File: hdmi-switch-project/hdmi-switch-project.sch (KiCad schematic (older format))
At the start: 0 parts

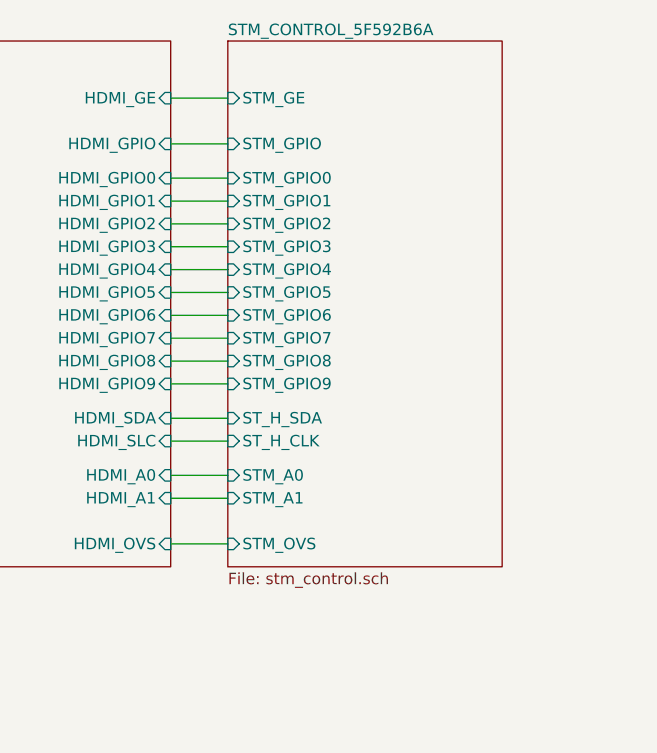
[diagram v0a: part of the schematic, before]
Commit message: added OVS jumper
Signed-off-by: Andrej Manduch <amanduch@gmail.com>
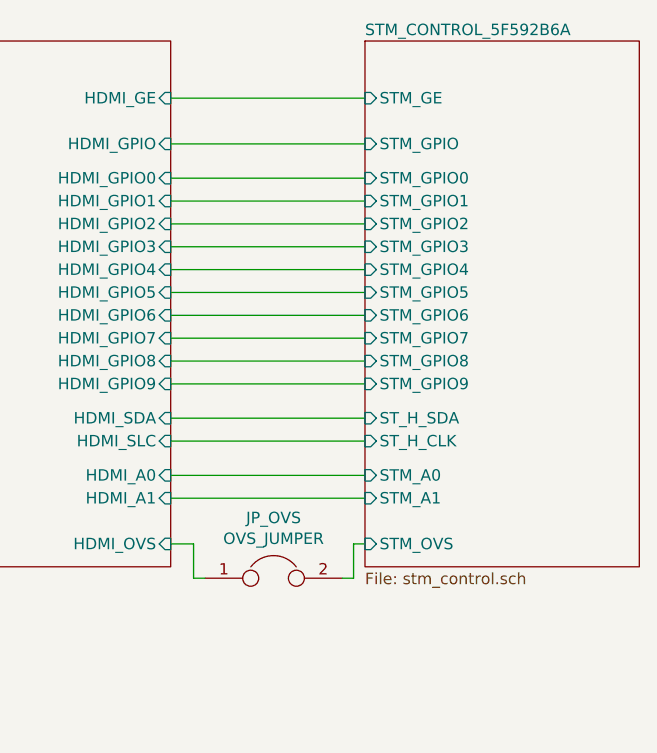
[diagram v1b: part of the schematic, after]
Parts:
- added JP_OVS: OVS_JUMPER, symbol Device:Jumper
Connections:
- net HDMI_CIRCUIT_F9FB5DE/HDMI_OVS: now also JP_OVS.1
- new net STM_CONTROL_5F592B6A/STM_OVS: JP_OVS.2
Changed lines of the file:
@@
 $EndSheet
 Wire Wire Line
-	6300 3050 6050 3050
+	6900 3050 6050 3050
 Wire Wire Line
-	6050 3150 6300 3150
+	6050 3150 6900 3150
 Wire Wire Line
-	6300 2900 6050 2900
+	6900 2900 6050 2900
 Wire Wire Line
-	6050 2800 6300 2800
+	6050 2800 6900 2800
 Wire Wire Line
-	6300 2450 6050 2450
+	6900 2450 6050 2450
 Wire Wire Line
-	6050 2350 6300 2350
+	6050 2350 6900 2350
 Wire Wire Line
-	6300 2250 6050 2250
+	6900 2250 6050 2250
 Wire Wire Line
-	6050 2150 6300 2150
+	6050 2150 6900 2150
 Wire Wire Line
-	6300 2050 6050 2050
+	6900 2050 6050 2050
 Wire Wire Line
-	6050 1950 6300 1950
+	6050 1950 6900 1950
 Wire Wire Line
-	6300 1850 6050 1850
+	6900 1850 6050 1850
 Wire Wire Line
-	6050 1750 6300 1750
+	6050 1750 6900 1750
 Wire Wire Line
-	6300 1600 6050 1600
+	6900 1600 6050 1600
 Wire Wire Line
-	6050 1400 6300 1400
+	6050 1400 6900 1400
 $Sheet
-S 6300 1150 1200 2300
+S 6900 1150 1200 2300
 U 5F592B6A
 F0 "STM_CONTROL_5F592B6A" 50
 F1 "stm_control.sch" 50
-F2 "ST_H_CLK" I L 6300 2900 50
-F3 "ST_H_SDA" I L 6300 2800 50
-F4 "STM_GPIO0" I L 6300 1750 50
-F5 "STM_GPIO1" I L 6300 1850 50
-F6 "STM_GPIO2" I L 6300 1950 50
-F7 "STM_GPIO3" I L 6300 2050 50
-F8 "STM_GPIO4" I L 6300 2150 50
-F9 "STM_GPIO5" I L 6300 2250 50
-F10 "STM_GPIO6" I L 6300 2350 50
-F11 "STM_GPIO7" I L 6300 2450 50
-F12 "STM_GPIO" I L 6300 1600 50
-F13 "STM_GE" I L 6300 1400 50
-F14 "STM_A0" I L 6300 3050 50
-F15 "STM_A1" I L 6300 3150 50
-F16 "STM_GPIO8" I L 6300 2550 50
-F17 "STM_GPIO9" I L 6300 2650 50
-F18 "STM_OVS" I L 6300 3350 50
+F2 "ST_H_CLK" I L 6900 2900 50
+F3 "ST_H_SDA" I L 6900 2800 50
+F4 "STM_GPIO0" I L 6900 1750 50
+F5 "STM_GPIO1" I L 6900 1850 50
+F6 "STM_GPIO2" I L 6900 1950 50
+F7 "STM_GPIO3" I L 6900 2050 50
+F8 "STM_GPIO4" I L 6900 2150 50
+F9 "STM_GPIO5" I L 6900 2250 50
+F10 "STM_GPIO6" I L 6900 2350 50
+F11 "STM_GPIO7" I L 6900 2450 50
+F12 "STM_GPIO" I L 6900 1600 50
+F13 "STM_GE" I L 6900 1400 50
+F14 "STM_A0" I L 6900 3050 50
+F15 "STM_A1" I L 6900 3150 50
+F16 "STM_GPIO8" I L 6900 2550 50
+F17 "STM_GPIO9" I L 6900 2650 50
+F18 "STM_OVS" I L 6900 3350 50
 $EndSheet
 Wire Wire Line
-	6300 3350 6050 3350
+	6050 2650 6900 2650
 Wire Wire Line
-	6050 2650 6300 2650
-Wire Wire Line
-	6300 2550 6050 2550
+	6900 2550 6050 2550
 $Comp
 L power:GND #PWR?
@@
 Wire Wire Line
 	3000 4150 3000 4200
+$Comp
+L Device:Jumper JP_OVS
+U 1 1 60C790A5
+P 6500 3500
+F 0 "JP_OVS" H 6500 3764 50  0000 C CNN
+F 1 "OVS_JUMPER" H 6500 3673 50  0000 C CNN
+F 2 "" H 6500 3500 50  0001 C CNN
+F 3 "~" H 6500 3500 50  0001 C CNN
+	1    6500 3500
+	1    0    0    -1
+$EndComp
+Wire Wire Line
+	6800 3500 6850 3500
+Wire Wire Line
+	6850 3500 6850 3350
+Wire Wire Line
+	6850 3350 6900 3350
+Wire Wire Line
+	6200 3500 6150 3500
+Wire Wire Line
+	6150 3500 6150 3350
+Wire Wire Line
+	6150 3350 6050 3350
 $EndSCHEMATC

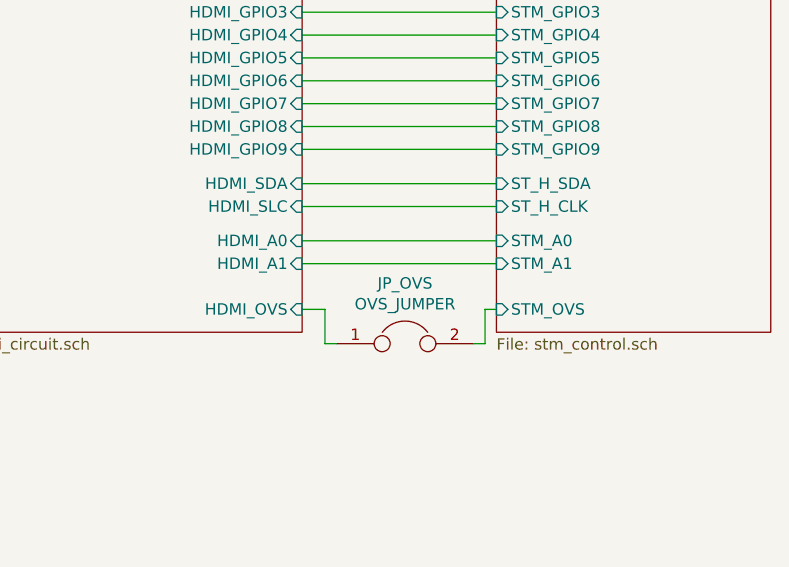
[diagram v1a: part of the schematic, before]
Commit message: Cosmetical changes, and VSDJ pin fixup
Signed-off-by: Andrej Manduch <amanduch@gmail.com>
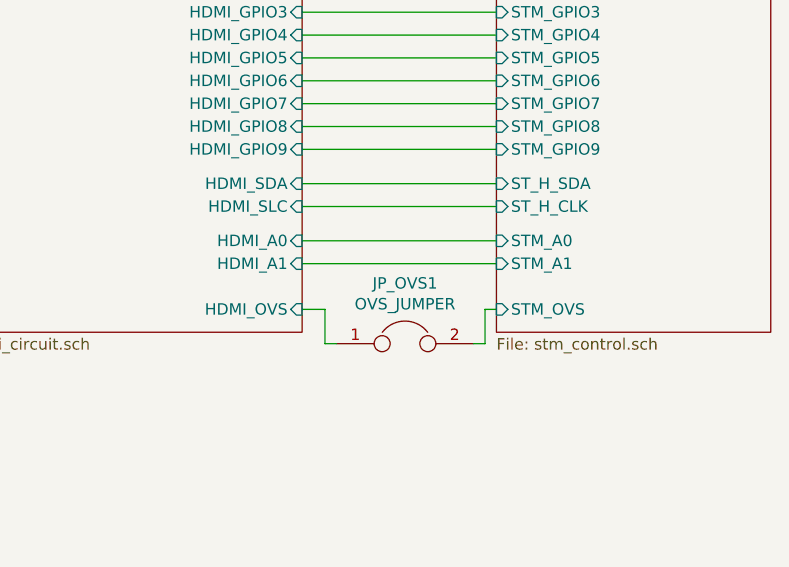
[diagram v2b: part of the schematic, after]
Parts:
- renumbered JP_OVS to JP_OVS1
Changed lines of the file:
@@
 EELAYER 30 0
 EELAYER END
-$Descr A3 11693 16535 portrait
+$Descr A3 16535 11693
 encoding utf-8
 Sheet 1 4
-Title ""
-Date ""
+Title "HDMI Switch 4:2 modul"
+Date "2020-06-30"
 Rev ""
 Comp ""
-Comment1 ""
+Comment1 "Devel board"
 Comment2 ""
 Comment3 ""
@@
 	6900 2550 6050 2550
 $Comp
-L power:GND #PWR?
+L power:GND #PWR0101
 U 1 1 60C19124
 P 3000 4200
-F 0 "#PWR?" H 3000 3950 50  0001 C CNN
+F 0 "#PWR0101" H 3000 3950 50  0001 C CNN
 F 1 "GND" H 3005 4027 50  0000 C CNN
 F 2 "" H 3000 4200 50  0001 C CNN
@@
 	3000 4150 3000 4200
 $Comp
-L Device:Jumper JP_OVS
+L Device:Jumper JP_OVS1
 U 1 1 60C790A5
 P 6500 3500
-F 0 "JP_OVS" H 6500 3764 50  0000 C CNN
+F 0 "JP_OVS1" H 6500 3764 50  0000 C CNN
 F 1 "OVS_JUMPER" H 6500 3673 50  0000 C CNN
 F 2 "" H 6500 3500 50  0001 C CNN

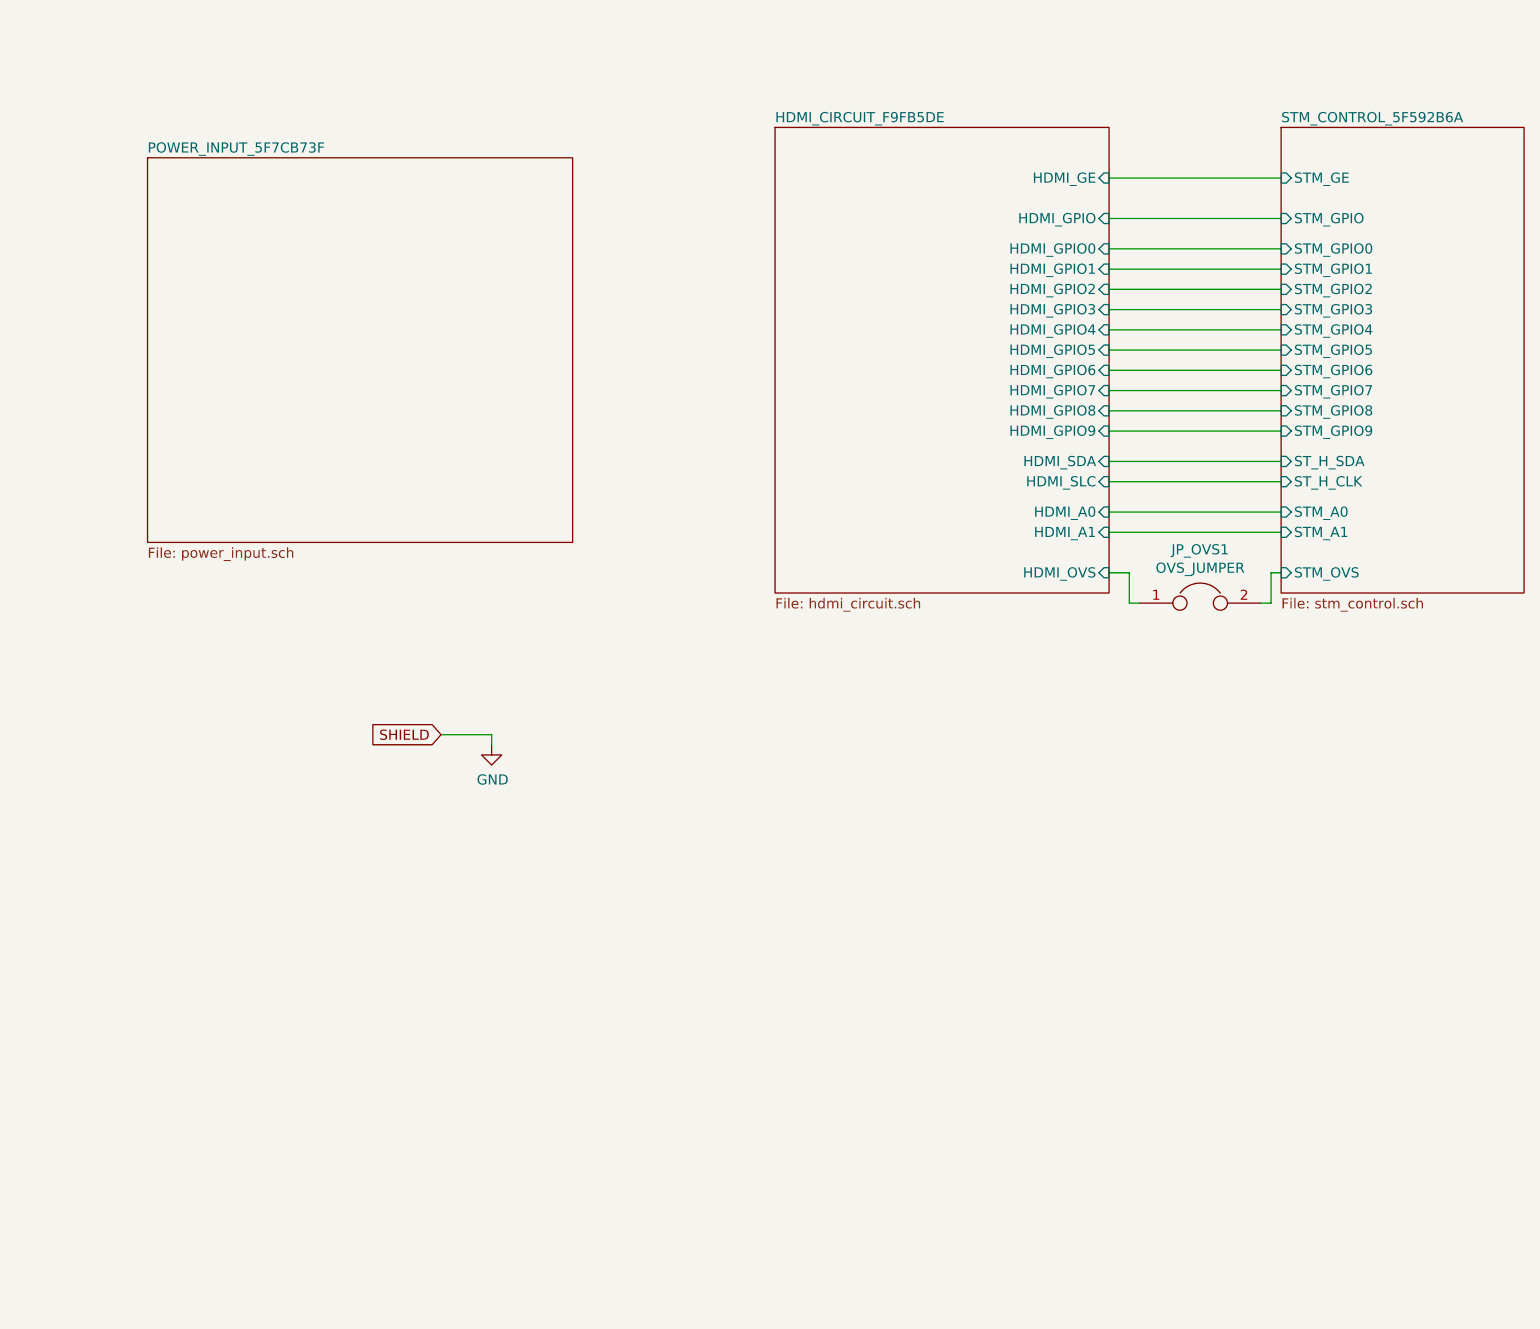
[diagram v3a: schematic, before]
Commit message: Added 2k resistor between GPIO ports
Signed-off-by: Andrej Manduch <amanduch@gmail.com>
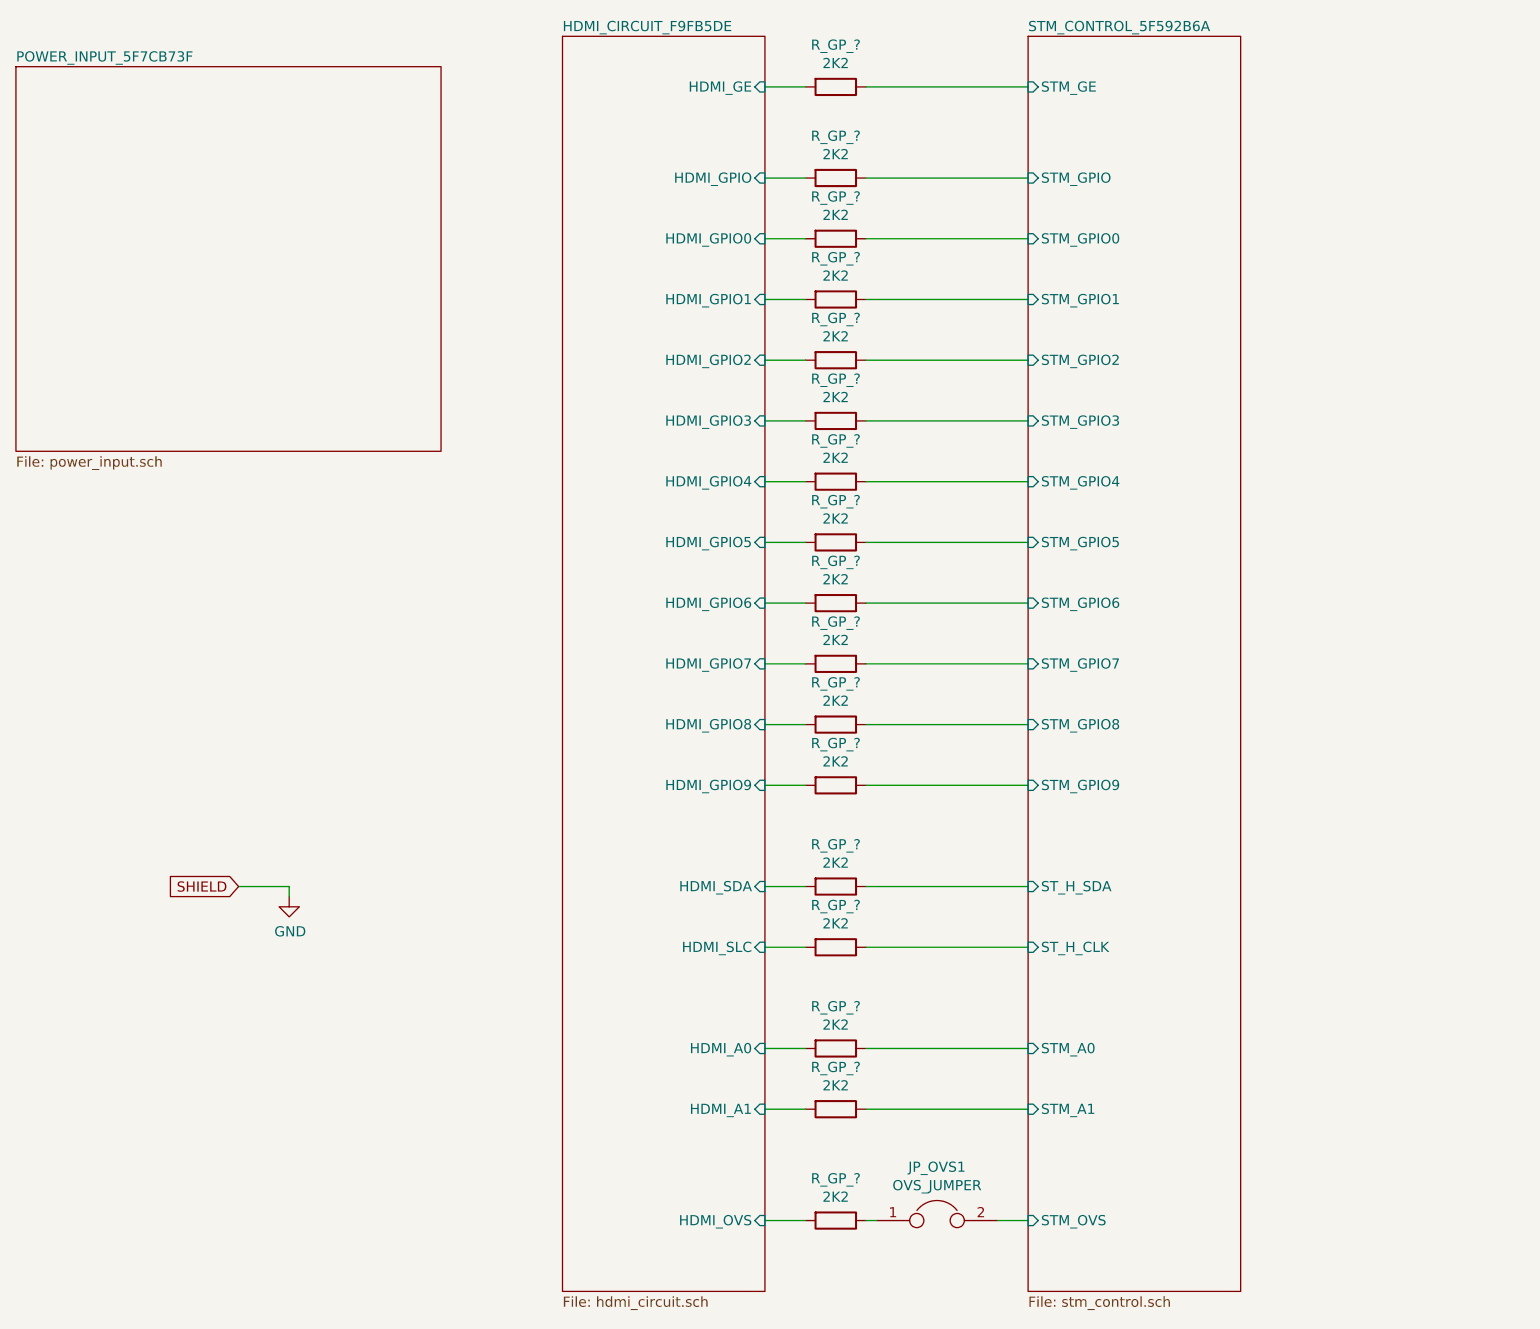
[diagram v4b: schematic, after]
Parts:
- added R_GP_? (x17): 2K2, symbol Device:R
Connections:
- net HDMI_CIRCUIT_F9FB5DE/HDMI_A0: now also R_GP_?.2
- net HDMI_CIRCUIT_F9FB5DE/HDMI_A1: now also R_GP_?.2
- net HDMI_CIRCUIT_F9FB5DE/HDMI_GE: now also R_GP_?.2
- net HDMI_CIRCUIT_F9FB5DE/HDMI_GPIO: now also R_GP_?.2
- net HDMI_CIRCUIT_F9FB5DE/HDMI_GPIO0: now also R_GP_?.2
- net HDMI_CIRCUIT_F9FB5DE/HDMI_GPIO1: now also R_GP_?.2
- net HDMI_CIRCUIT_F9FB5DE/HDMI_GPIO2: now also R_GP_?.2
- net HDMI_CIRCUIT_F9FB5DE/HDMI_GPIO3: now also R_GP_?.2
- net HDMI_CIRCUIT_F9FB5DE/HDMI_GPIO4: now also R_GP_?.2
- net HDMI_CIRCUIT_F9FB5DE/HDMI_GPIO5: now also R_GP_?.2
- net HDMI_CIRCUIT_F9FB5DE/HDMI_GPIO6: now also R_GP_?.2
- net HDMI_CIRCUIT_F9FB5DE/HDMI_GPIO7: now also R_GP_?.2
- net HDMI_CIRCUIT_F9FB5DE/HDMI_GPIO8: now also R_GP_?.2
- net HDMI_CIRCUIT_F9FB5DE/HDMI_GPIO9: now also R_GP_?.2
- net HDMI_CIRCUIT_F9FB5DE/HDMI_OVS: now also R_GP_?.2; no longer JP_OVS1.1
- net HDMI_CIRCUIT_F9FB5DE/HDMI_SDA: now also R_GP_?.2
- net HDMI_CIRCUIT_F9FB5DE/HDMI_SLC: now also R_GP_?.2
- new net: JP_OVS1.1, R_GP_?.1
- new net STM_CONTROL_5F592B6A/STM_A0: R_GP_?.1
- new net STM_CONTROL_5F592B6A/STM_A1: R_GP_?.1
- new net STM_CONTROL_5F592B6A/STM_GE: R_GP_?.1
- new net STM_CONTROL_5F592B6A/STM_GPIO: R_GP_?.1
- new net STM_CONTROL_5F592B6A/STM_GPIO0: R_GP_?.1
- new net STM_CONTROL_5F592B6A/STM_GPIO1: R_GP_?.1
- new net STM_CONTROL_5F592B6A/STM_GPIO2: R_GP_?.1
- new net STM_CONTROL_5F592B6A/STM_GPIO3: R_GP_?.1
- new net STM_CONTROL_5F592B6A/STM_GPIO4: R_GP_?.1
- new net STM_CONTROL_5F592B6A/STM_GPIO5: R_GP_?.1
- new net STM_CONTROL_5F592B6A/STM_GPIO6: R_GP_?.1
- new net STM_CONTROL_5F592B6A/STM_GPIO7: R_GP_?.1
- new net STM_CONTROL_5F592B6A/STM_GPIO8: R_GP_?.1
- new net STM_CONTROL_5F592B6A/STM_GPIO9: R_GP_?.1
- new net STM_CONTROL_5F592B6A/ST_H_CLK: R_GP_?.1
- new net STM_CONTROL_5F592B6A/ST_H_SDA: R_GP_?.1
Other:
- moved on the sheet: JP_OVS1
